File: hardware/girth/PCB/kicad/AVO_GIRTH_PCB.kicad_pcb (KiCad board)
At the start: 4 copper layers, 65.5 x 43.5 mm, 115 parts, among them J1 USB-C 16P, J2 BATERÍA 1S, K1 G6KU-2F-Y DC3, Q1 AO3401A, Q10 AO3401A, Q11 AO3400A, Q12 2N7002, Q13 AO3400A, Q14 AO3401A, Q15 2N7002, Q16 2N7002, Q2 AO3401A, Q3 AO3401A, SW1 REED (1), SW2 REED (2), U1 BQ51013BRHLR, U2 BQ24072RGTR, U3 RT9080-33GJ5, U4 ESP32-C6-MINI-1U-N4, U5 BNO085, U6 USBLC6-2SC6, Y1 32,768 kHz 12,5 pF

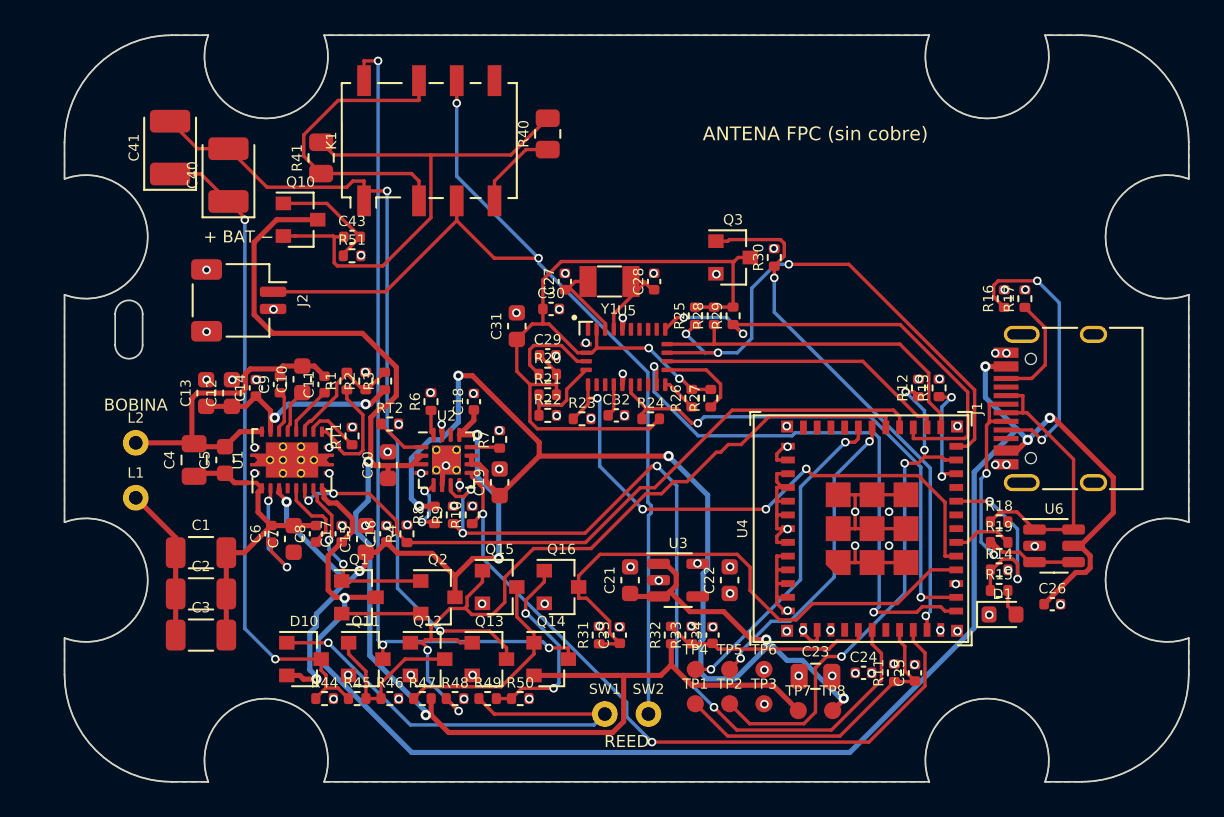
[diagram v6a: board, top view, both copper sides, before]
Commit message: PCB cincha: DRC/ERC, Gerber y renders de KiCad 9 [skip ci]
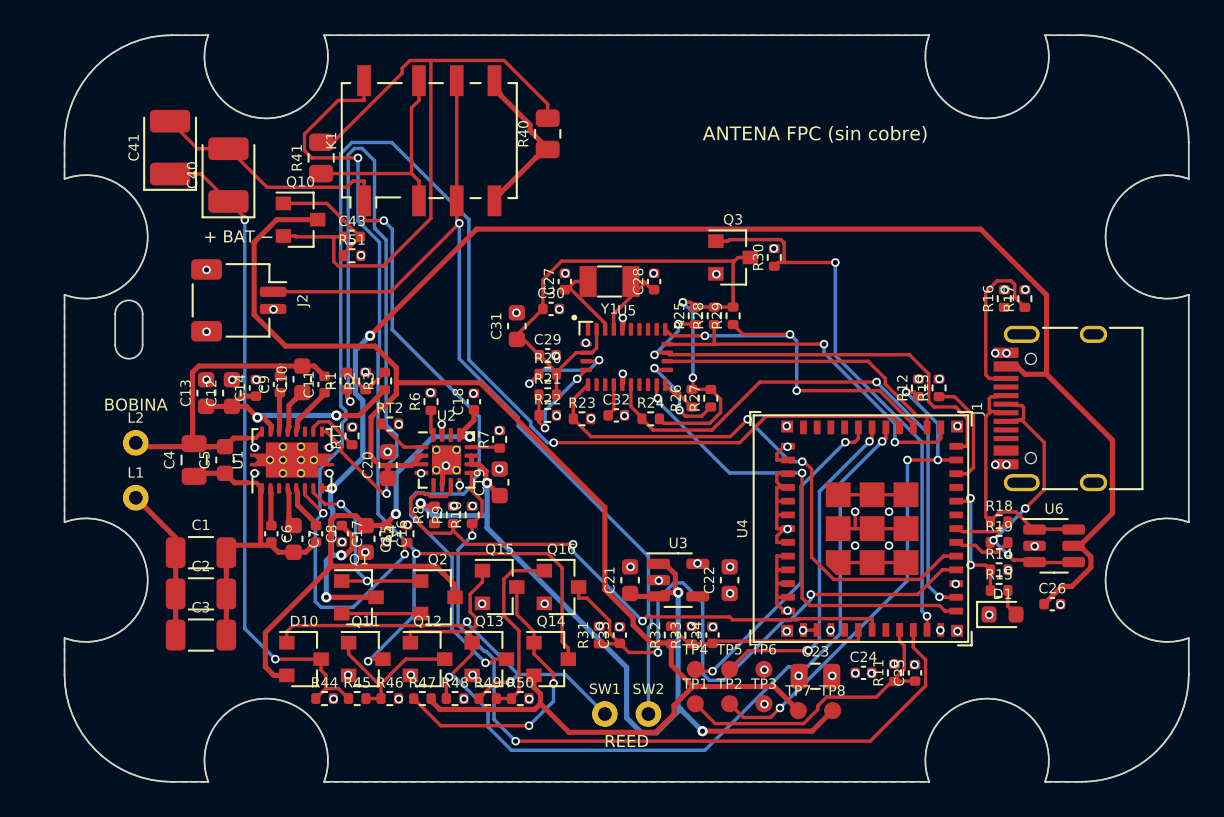
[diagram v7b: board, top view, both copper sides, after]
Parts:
- turned C15 to -90 degrees
- turned C16 to -90 degrees
- turned C17 to -90 degrees
- turned C6 to -90 degrees
- turned C7 to -90 degrees
- turned C8 to -90 degrees
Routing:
- net QI_CHG: track 41.0 -> 82.4 mm, vias 2 -> 3
- net QI_ILIM: track 7.05 -> 42.8 mm, vias 0 -> 2
- net VSYS: track 68.9 -> 51.4 mm, vias 5 -> 4
- net CC1: track 16.7 -> 0.00 mm, vias 2 -> 0
- net CHG_PG: track 48.4 -> 35.0 mm, vias 4 -> 2
- net IMU_VDD: track 51.9 -> 42.8 mm
- net BAT_SW: track 30.0 -> 38.3 mm
- net K_B: track 48.6 -> 56.9 mm
- net RLY_OFF: track 46.3 -> 53.9 mm
- net BAT_RAW: track 60.9 -> 54.2 mm, vias 2 -> 1
- net RLY_NC: track 18.4 -> 12.6 mm
- net IMU_CS: track 32.0 -> 26.4 mm, vias 3 -> 2
- net IMU_MISO: track 27.7 -> 22.2 mm, vias 2 -> 3
- net CHG_STAT: track 41.7 -> 46.7 mm
- net QI_BOOT1: track 6.93 -> 2.17 mm, vias 2 -> 0
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
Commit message: PCB cincha: DRC/ERC, Gerber y renders de KiCad 9 [skip ci]
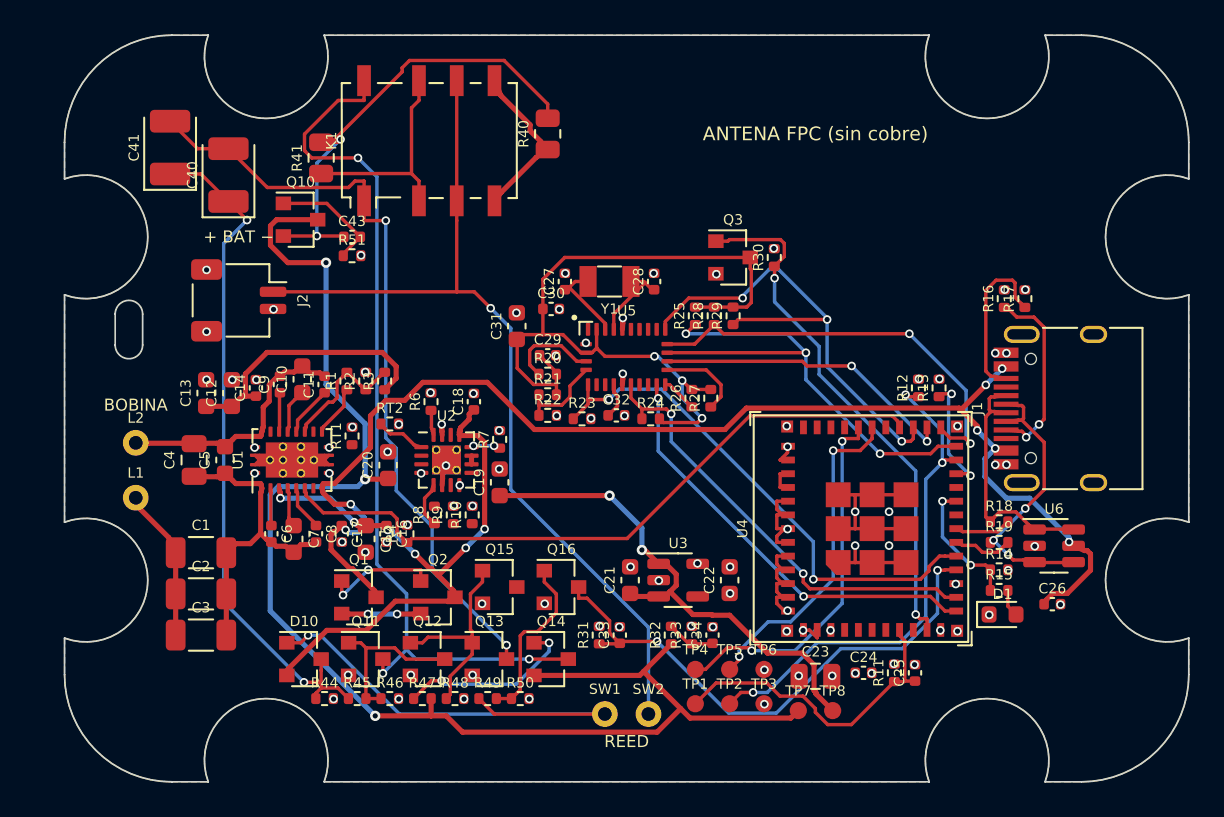
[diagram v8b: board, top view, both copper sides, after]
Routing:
- net CHG_STAT: track 46.7 -> 0.00 mm, vias 2 -> 0
- net QI_CHG: track 82.4 -> 40.1 mm, vias 3 -> 0
- net RLY_OFF: track 53.9 -> 12.1 mm, vias 2 -> 0
- net QI_ILIM: track 42.8 -> 3.00 mm, vias 2 -> 0
- net CHG_PG: track 35.0 -> 0.00 mm, vias 2 -> 0
- net VSYS: track 51.4 -> 30.4 mm, vias 4 -> 2
- net VBUS: track 91.8 -> 76.7 mm, vias 4 -> 7
- net CC1: track 0.00 -> 11.0 mm, vias 0 -> 2
- net BAT_SW: track 38.3 -> 27.8 mm, vias 0 -> 2
- net BAT_ADC: track 12.0 -> 2.83 mm
- net QI_AC2: track 21.7 -> 14.6 mm
- net RLY_PG: track 16.9 -> 10.6 mm
- net IMU_MISO: track 22.2 -> 28.4 mm
- net IMU_RST: track 32.4 -> 26.3 mm
- net K_A: track 51.0 -> 45.1 mm
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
